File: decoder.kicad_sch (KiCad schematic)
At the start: 4 parts, among them U12 74HCT138, U19 74HCT30

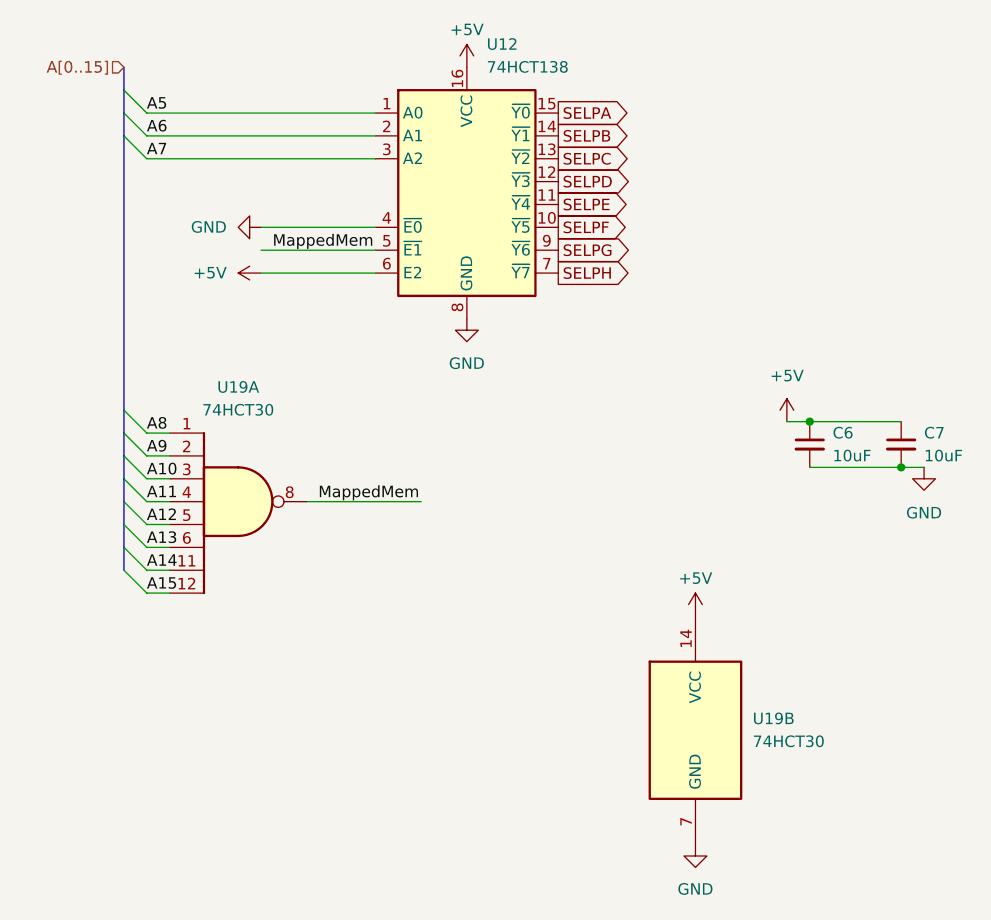
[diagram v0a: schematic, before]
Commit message: disambiguate register address
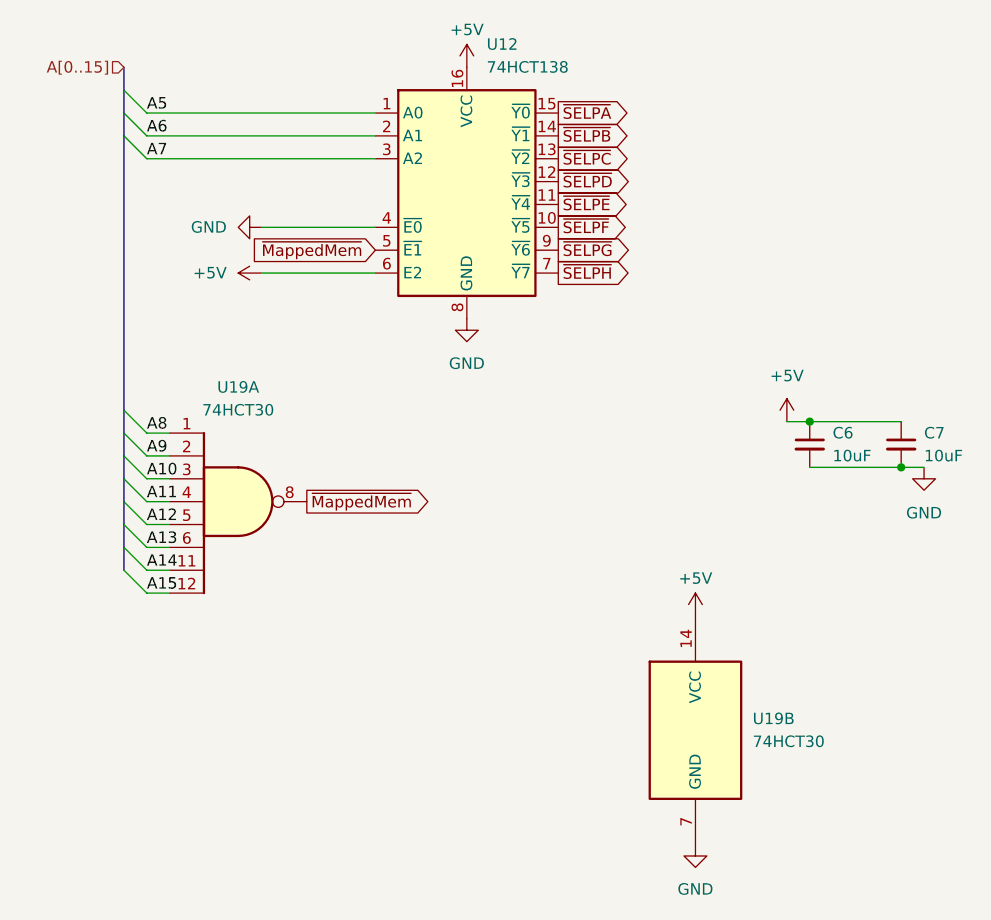
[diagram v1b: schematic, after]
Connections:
- net MappedMem renamed ~{MappedMem}
- net SELPA renamed ~{SELPA}
- net SELPB renamed ~{SELPB}
- net SELPC renamed ~{SELPC}
- net SELPD renamed ~{SELPD}
- net SELPE renamed ~{SELPE}
- net SELPF renamed ~{SELPF}
- net SELPG renamed ~{SELPG}
- net SELPH renamed ~{SELPH}
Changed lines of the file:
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@@
-		)
-	)
-	(wire
-		(pts
-			(xy 64.77 86.36) (xy 77.47 86.36)
-		)
-		(stroke
-			(width 0)
-			(type default)
 		)
 	)
@@
 		(pts
 			(xy 130.81 82.55) (xy 133.35 82.55)
-		)
-		(stroke
-			(width 0)
-			(type default)
-		)
-	)
-	(wire
-		(pts
-			(xy 59.69 58.42) (xy 72.39 58.42)
 		)
 		(stroke
@@
 		)
 	)
-	(label "MappedMem"
-		(at 66.04 86.36 0)
-		(fields_autoplaced yes)
-		(effects
-			(font
-				(size 1.27 1.27)
-			)
-			(justify left bottom)
-		)
-	)
 	(label "A15"
 		(at 46.99 96.52 0)
@@
 		)
 	)
-	(label "MappedMem"
-		(at 60.96 58.42 0)
-		(fields_autoplaced yes)
-		(effects
-			(font
-				(size 1.27 1.27)
-			)
-			(justify left bottom)
-		)
-	)
 	(label "A10"
 		(at 46.99 83.82 0)
@@
 		)
 	)
-	(global_label "SELPC"
+	(global_label "~{SELPC}"
 		(shape output)
 		(at 92.71 48.26 0)
@@
 		)
 	)
-	(global_label "SELPA"
+	(global_label "~{MappedMem}"
+		(shape input)
+		(at 72.39 58.42 180)
+		(fields_autoplaced yes)
+		(effects
+			(font
+				(size 1.27 1.27)
+			)
+			(justify right)
+		)
+		(property "Intersheetrefs" "${INTERSHEET_REFS}"
+			(at 58.0355 58.42 0)
+			(effects
+				(font
+					(size 1.27 1.27)
+				)
+				(justify right)
+				(hide yes)
+			)
+		)
+	)
+	(global_label "~{SELPA}"
 		(shape output)
 		(at 92.71 43.18 0)
@@
 		)
 	)
-	(global_label "SELPE"
+	(global_label "~{SELPE}"
 		(shape output)
 		(at 92.71 53.34 0)
@@
 		)
 	)
-	(global_label "SELPF"
+	(global_label "~{MappedMem}"
+		(shape output)
+		(at 64.77 86.36 0)
+		(fields_autoplaced yes)
+		(effects
+			(font
+				(size 1.27 1.27)
+			)
+			(justify left)
+		)
+		(property "Intersheetrefs" "${INTERSHEET_REFS}"
+			(at 79.1245 86.36 0)
+			(effects
+				(font
+					(size 1.27 1.27)
+				)
+				(justify left)
+				(hide yes)
+			)
+		)
+	)
+	(global_label "~{SELPF}"
 		(shape output)
 		(at 92.71 55.88 0)
@@
 		)
 	)
-	(global_label "SELPB"
+	(global_label "~{SELPB}"
 		(shape output)
 		(at 92.71 45.72 0)
@@
 		)
 	)
-	(global_label "SELPG"
+	(global_label "~{SELPG}"
 		(shape output)
 		(at 92.71 58.42 0)
@@
 		)
 	)
-	(global_label "SELPH"
+	(global_label "~{SELPH}"
 		(shape output)
 		(at 92.71 60.96 0)
@@
 		)
 	)
-	(global_label "SELPD"
+	(global_label "~{SELPD}"
 		(shape output)
 		(at 92.71 50.8 0)

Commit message: clean up before redesign
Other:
- moved on the sheet: U19B
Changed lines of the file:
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@@
 (kicad_sch
-	(version 20231120)
+	(version 20250114)
 	(generator "eeschema")
-	(generator_version "8.0")
+	(generator_version "9.0")
 	(paper "A4")
 	(title_block
@@
 	(label "A5"
 		(at 46.99 43.18 0)
-		(fields_autoplaced yes)
 		(effects
 			(font
@@
 	(label "A15"
 		(at 46.99 96.52 0)
-		(fields_autoplaced yes)
 		(effects
 			(font
@@
 	(label "A7"
 		(at 46.99 48.26 0)
-		(fields_autoplaced yes)
 		(effects
 			(font
@@
 	(label "A8"
 		(at 46.99 78.74 0)
-		(fields_autoplaced yes)
 		(effects
 			(font
@@
 	(label "A12"
 		(at 46.99 88.9 0)
-		(fields_autoplaced yes)
 		(effects
 			(font
@@
 	(label "A11"
 		(at 46.99 86.36 0)
-		(fields_autoplaced yes)
 		(effects
 			(font
@@
 	(label "A13"
 		(at 46.99 91.44 0)
-		(fields_autoplaced yes)
 		(effects
 			(font
@@
 	(label "A14"
 		(at 46.99 93.98 0)
-		(fields_autoplaced yes)
 		(effects
 			(font
@@
 	(label "A9"
 		(at 46.99 81.28 0)
-		(fields_autoplaced yes)
 		(effects
 			(font
@@
 	(label "A6"
 		(at 46.99 45.72 0)
-		(fields_autoplaced yes)
 		(effects
 			(font
@@
 	(label "A10"
 		(at 46.99 83.82 0)
-		(fields_autoplaced yes)
 		(effects
 			(font
@@
 		(shape input)
 		(at 44.45 38.1 180)
-		(fields_autoplaced yes)
 		(effects
 			(font
@@
 		(lib_name "GND_1")
 		(lib_id "power:GND")
-		(at 107.95 124.46 0)
+		(at 121.92 120.65 0)
 		(unit 1)
 		(exclude_from_sim no)
@@
 		(fields_autoplaced yes)
 		(property "Reference" "#PWR051"
-			(at 107.95 130.81 0)
+			(at 121.92 127 0)
 			(effects
 				(font
@@
 		)
 		(property "Value" "GND"
-			(at 107.95 129.4384 0)
+			(at 121.92 125.6284 0)
 			(effects
 				(font
@@
 		)
 		(property "Footprint" ""
-			(at 107.95 124.46 0)
+			(at 121.92 120.65 0)
 			(effects
 				(font
@@
 		)
 		(property "Datasheet" ""
-			(at 107.95 124.46 0)
+			(at 121.92 120.65 0)
 			(effects
 				(font
@@
 		)
 		(property "Description" ""
-			(at 107.95 124.46 0)
+			(at 121.92 120.65 0)
 			(effects
 				(font
@@
 		(lib_name "+5V_1")
 		(lib_id "power:+5V")
-		(at 107.95 99.06 0)
+		(at 121.92 95.25 0)
 		(unit 1)
 		(exclude_from_sim no)
@@
 		(fields_autoplaced yes)
 		(property "Reference" "#PWR050"
-			(at 107.95 102.87 0)
+			(at 121.92 99.06 0)
 			(effects
 				(font
@@
 		)
 		(property "Value" "+5V"
-			(at 107.95 94.8944 0)
+			(at 121.92 91.0844 0)
 			(effects
 				(font
@@
 		)
 		(property "Footprint" ""
-			(at 107.95 99.06 0)
+			(at 121.92 95.25 0)
 			(effects
 				(font
@@
 		)
 		(property "Datasheet" ""
-			(at 107.95 99.06 0)
+			(at 121.92 95.25 0)
 			(effects
 				(font
@@
 		)
 		(property "Description" ""
-			(at 107.95 99.06 0)
+			(at 121.92 95.25 0)
 			(effects
 				(font
@@
 	(symbol
 		(lib_id "74xx:74LS30")
-		(at 107.95 111.76 0)
+		(at 121.92 107.95 0)
 		(unit 2)
 		(exclude_from_sim no)
@@
 		(fields_autoplaced yes)
 		(property "Reference" "U19"
-			(at 114.3 110.4899 0)
+			(at 128.27 106.6799 0)
 			(effects
 				(font
@@
 		)
 		(property "Value" "74HCT30"
-			(at 114.3 113.0299 0)
+			(at 128.27 109.2199 0)
 			(effects
 				(font
@@
 		)
 		(property "Footprint" "Package_SO:SOIC-14_3.9x8.7mm_P1.27mm"
-			(at 107.95 111.76 0)
+			(at 121.92 107.95 0)
 			(effects
 				(font
@@
 		)
 		(property "Datasheet" "http://www.ti.com/lit/gpn/sn74LS30"
-			(at 107.95 111.76 0)
+			(at 121.92 107.95 0)
 			(effects
 				(font
@@
 		)
 		(property "Description" "8-input NAND"
-			(at 107.95 111.76 0)
-			(effects
-				(font
+			(at 121.92 107.95 0)
+			(effects
+				(font
